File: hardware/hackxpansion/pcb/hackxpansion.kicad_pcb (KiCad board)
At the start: 4 copper layers, 52 x 69 mm, 101 parts, among them CN1 533981471, CN2 533981471, CN3 533981471, CN4 533981471, IC1 ADS7128IRTET, J1 Conn_01x03_MountingPin, J2 USB_C_Receptacle_USB2.0_14P, Q1 BSS138, Q2 2N7002, SW1 SW_Push, SW2 SW_Push, SW3 SW_On_Off, U2 RP2354B, U5 SPX3819M5-L-3-3, U7 BQ24075RGT, U8 USBLC6-2SC6, Y1 ABM8-272-T3

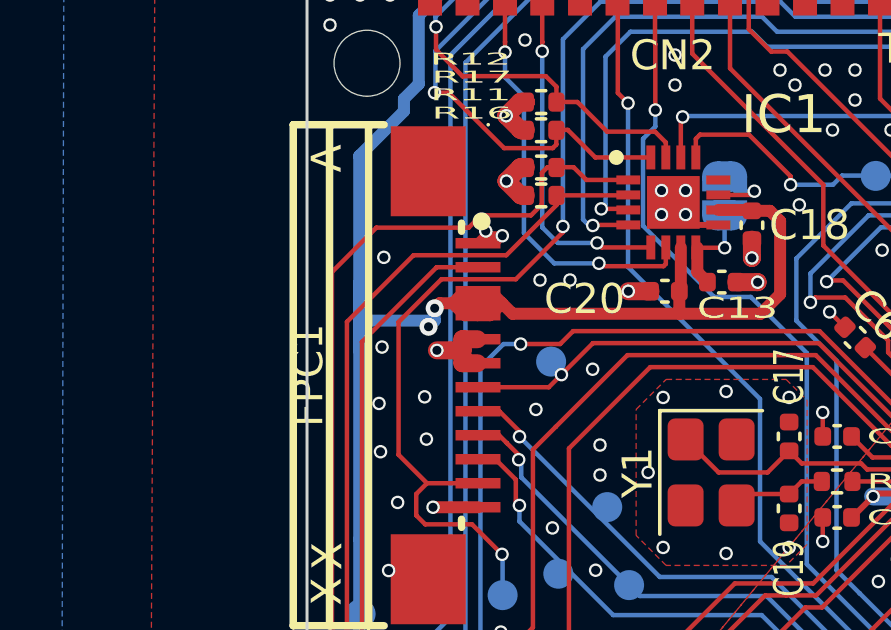
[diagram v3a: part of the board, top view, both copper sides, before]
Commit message: fixed unconnected 3v3 via next to display
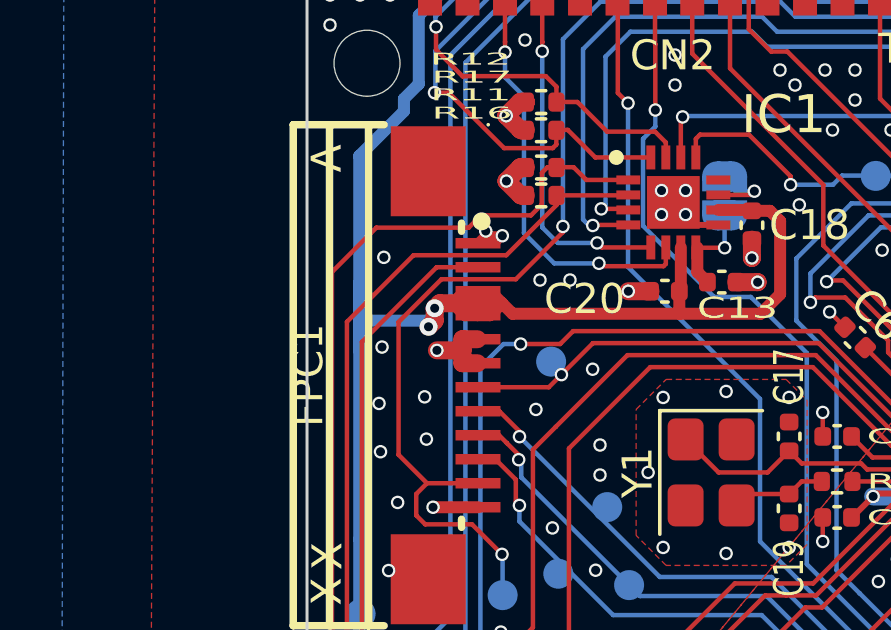
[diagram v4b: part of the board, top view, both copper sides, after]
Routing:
- net /+3V3: track 294.9 -> 295.6 mm
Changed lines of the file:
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@@
+	)
+	(segment
+		(start 106.73 72.9)
+		(end 106.29246 72.9)
+		(width 0.6)
+		(layer "F.Cu")
+		(net "/+3V3")
 	)
 	(segment
@@
 	)
 	(segment
+		(start 134.779998 63.587538)
+		(end 134.779998 62.66)
+		(width 0.4)
+		(layer "F.Cu")
+		(net "/+3V3")
+	)
+	(segment
+		(start 114.290003 73.25)
+		(end 116.99 73.25)
+		(width 0.4)
+		(layer "F.Cu")
+		(net "/+3V3")
+	)
+	(segment
+		(start 127.340001 85.24)
+		(end 127.340002 86.159999)
+		(width 0.15)
+		(layer "F.Cu")
+		(net "/+3V3")
+	)
+	(segment
+		(start 123.195 96.015001)
+		(end 123.195 96.782538)
+		(width 0.4)
+		(layer "F.Cu")
+		(net "/+3V3")
+	)
+	(segment
+		(start 132.736502 76.439999)
+		(end 133.440002 76.440001)
+		(width 0.15)
+		(layer "F.Cu")
+		(net "/+3V3")
+	)
+	(segment
+		(start 108.37 72.9)
+		(end 108.02 72.55)
+		(width 0.4)
+		(layer "F.Cu")
+		(net "/+3V3")
+	)
+	(segment
+		(start 134.588768 63.778768)
+		(end 134.779998 63.587538)
+		(width 0.4)
+		(layer "F.Cu")
+		(net "/+3V3")
+	)
+	(segment
+		(start 130.040002 73.743499)
+		(end 130.040003 74.54)
+		(width 0.2)
+		(layer "F.Cu")
+		(net "/+3V3")
+	)
+	(segment
+		(start 106.93 84.13)
+		(end 104.62 84.13)
+		(width 0.15)
+		(layer "F.Cu")
+		(net "/+3V3")
+	)
+	(segment
+		(start 151.21 97.136168)
+		(end 151.216029 97.142197)
+		(width 0.4)
+		(layer "F.Cu")
+		(net "/+3V3")
+	)
+	(segment
+		(start 107.13 73.3)
+		(end 106.73 72.9)
+		(width 0.4)
+		(layer "F.Cu")
+		(net "/+3V3")
+	)
+	(segment
+		(start 127.640002 83.536501)
+		(end 127.640001 84.94)
+		(width 0.15)
+		(layer "F.Cu")
+		(net "/+3V3")
+	)
+	(segment
+		(start 131.940002 79.639999)
+		(end 132.740003 79.64)
+		(width 0.2)
+		(layer "F.Cu")
+		(net "/+3V3")
+	)
+	(segment
+		(start 126.040002 73.743499)
+		(end 126.040003 72.64)
+		(width 0.15)
+		(layer "F.Cu")
+		(net "/+3V3")
+	)
+	(segment
+		(start 116.7 69.82)
+		(end 116.67 69.79)
+		(width 0.4)
+		(layer "F.Cu")
+		(net "/+3V3")
+	)
+	(segment
+		(start 124.040002 83.940001)
+		(end 123.340002 84.64)
+		(width 0.15)
+		(layer "F.Cu")
+		(net "/+3V3")
+	)
+	(segment
+		(start 105.920009 73.684293)
+		(end 106.125 73.479302)
+		(width 0.6)
+		(layer "F.Cu")
+		(net "/+3V3")
+	)
+	(segment
+		(start 133.190003 79.64)
+		(end 133.590002 79.240001)
+		(width 0.15)
+		(layer "F.Cu")
+		(net "/+3V3")
+	)
+	(segment
+		(start 132.140001 85.659999)
+		(end 132.140001 85.030001)
+		(width 0.15)
+		(layer "F.Cu")
+		(net "/+3V3")
+	)
+	(segment
+		(start 108.32 83.87)
+		(end 107.19 83.87)
+		(width 0.15)
+		(layer "F.Cu")
+		(net "/+3V3")
+	)
+	(segment
+		(start 114.33 72.45)
+		(end 114.33 71.04)
+		(width 0.4)
+		(layer "F.Cu")
+		(net "/+3V3")
+	)
+	(segment
+		(start 133.890002 81.16)
+		(end 133.810003 81.239999)
+		(width 0.2)
+		(layer "F.Cu")
+		(net "/+3V3")
+	)
+	(segment
+		(start 108.33 83.86)
+		(end 108.32 83.87)
+		(width 0.15)
+		(layer "F.Cu")
+		(net "/+3V3")
+	)
+	(segment
+		(start 117.3 69.82)
+		(end 116.7 69.82)
+		(width 0.4)
+		(layer "F.Cu")
+		(net "/+3V3")
+	)
+	(segment
 		(start 106.29246 72.9)
 		(end 106.125 73.06746)
-		(width 0.4)
-		(layer "F.Cu")
-		(net "/+3V3")
-	)
-	(segment
-		(start 134.779998 63.587538)
-		(end 134.779998 62.66)
-		(width 0.4)
-		(layer "F.Cu")
-		(net "/+3V3")
-	)
-	(segment
-		(start 114.290003 73.25)
-		(end 116.99 73.25)
-		(width 0.4)
-		(layer "F.Cu")
-		(net "/+3V3")
-	)
-	(segment
-		(start 127.340001 85.24)
-		(end 127.340002 86.159999)
-		(width 0.15)
-		(layer "F.Cu")
-		(net "/+3V3")
-	)
-	(segment
-		(start 123.195 96.015001)
-		(end 123.195 96.782538)
-		(width 0.4)
-		(layer "F.Cu")
-		(net "/+3V3")
-	)
-	(segment
-		(start 132.736502 76.439999)
-		(end 133.440002 76.440001)
-		(width 0.15)
-		(layer "F.Cu")
-		(net "/+3V3")
-	)
-	(segment
-		(start 108.37 72.9)
-		(end 108.02 72.55)
-		(width 0.4)
-		(layer "F.Cu")
-		(net "/+3V3")
-	)
-	(segment
-		(start 134.588768 63.778768)
-		(end 134.779998 63.587538)
-		(width 0.4)
-		(layer "F.Cu")
-		(net "/+3V3")
-	)
-	(segment
-		(start 130.040002 73.743499)
-		(end 130.040003 74.54)
-		(width 0.2)
-		(layer "F.Cu")
-		(net "/+3V3")
-	)
-	(segment
-		(start 106.93 84.13)
-		(end 104.62 84.13)
-		(width 0.15)
-		(layer "F.Cu")
-		(net "/+3V3")
-	)
-	(segment
-		(start 151.21 97.136168)
-		(end 151.216029 97.142197)
-		(width 0.4)
-		(layer "F.Cu")
-		(net "/+3V3")
-	)
-	(segment
-		(start 107.13 73.3)
-		(end 106.73 72.9)
-		(width 0.4)
-		(layer "F.Cu")
-		(net "/+3V3")
-	)
-	(segment
-		(start 127.640002 83.536501)
-		(end 127.640001 84.94)
-		(width 0.15)
-		(layer "F.Cu")
-		(net "/+3V3")
-	)
-	(segment
-		(start 131.940002 79.639999)
-		(end 132.740003 79.64)
-		(width 0.2)
-		(layer "F.Cu")
-		(net "/+3V3")
-	)
-	(segment
-		(start 126.040002 73.743499)
-		(end 126.040003 72.64)
-		(width 0.15)
-		(layer "F.Cu")
-		(net "/+3V3")
-	)
-	(segment
-		(start 116.7 69.82)
-		(end 116.67 69.79)
-		(width 0.4)
-		(layer "F.Cu")
-		(net "/+3V3")
-	)
-	(segment
-		(start 124.040002 83.940001)
-		(end 123.340002 84.64)
-		(width 0.15)
-		(layer "F.Cu")
-		(net "/+3V3")
-	)
-	(segment
-		(start 133.190003 79.64)
-		(end 133.590002 79.240001)
-		(width 0.15)
-		(layer "F.Cu")
-		(net "/+3V3")
-	)
-	(segment
-		(start 132.140001 85.659999)
-		(end 132.140001 85.030001)
-		(width 0.15)
-		(layer "F.Cu")
-		(net "/+3V3")
-	)
-	(segment
-		(start 108.32 83.87)
-		(end 107.19 83.87)
-		(width 0.15)
-		(layer "F.Cu")
-		(net "/+3V3")
-	)
-	(segment
-		(start 114.33 72.45)
-		(end 114.33 71.04)
-		(width 0.4)
-		(layer "F.Cu")
-		(net "/+3V3")
-	)
-	(segment
-		(start 133.890002 81.16)
-		(end 133.810003 81.239999)
-		(width 0.2)
-		(layer "F.Cu")
-		(net "/+3V3")
-	)
-	(segment
-		(start 108.33 83.86)
-		(end 108.32 83.87)
-		(width 0.15)
-		(layer "F.Cu")
-		(net "/+3V3")
-	)
-	(segment
-		(start 117.3 69.82)
-		(end 116.7 69.82)
-		(width 0.4)
+		(width 0.6)
 		(layer "F.Cu")
 		(net "/+3V3")
@@
 	)
 	(segment
+		(start 106.125 73.479302)
+		(end 106.125 73.06746)
+		(width 0.6)
+		(layer "F.Cu")
+		(net "/+3V3")
+	)
+	(segment
 		(start 148.079998 94.77)
 		(end 148.529998 95.22)
@@
 		(layer "F.Cu")
 		(net "/+3V3")
-	)
-	(segment
-		(start 106.73 72.9)
-		(end 106.29246 72.9)
-		(width 0.4)
-		(layer "F.Cu")
-		(net "/+3V3")

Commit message: updated led resistor
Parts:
- R25: value 10k -> 1k5

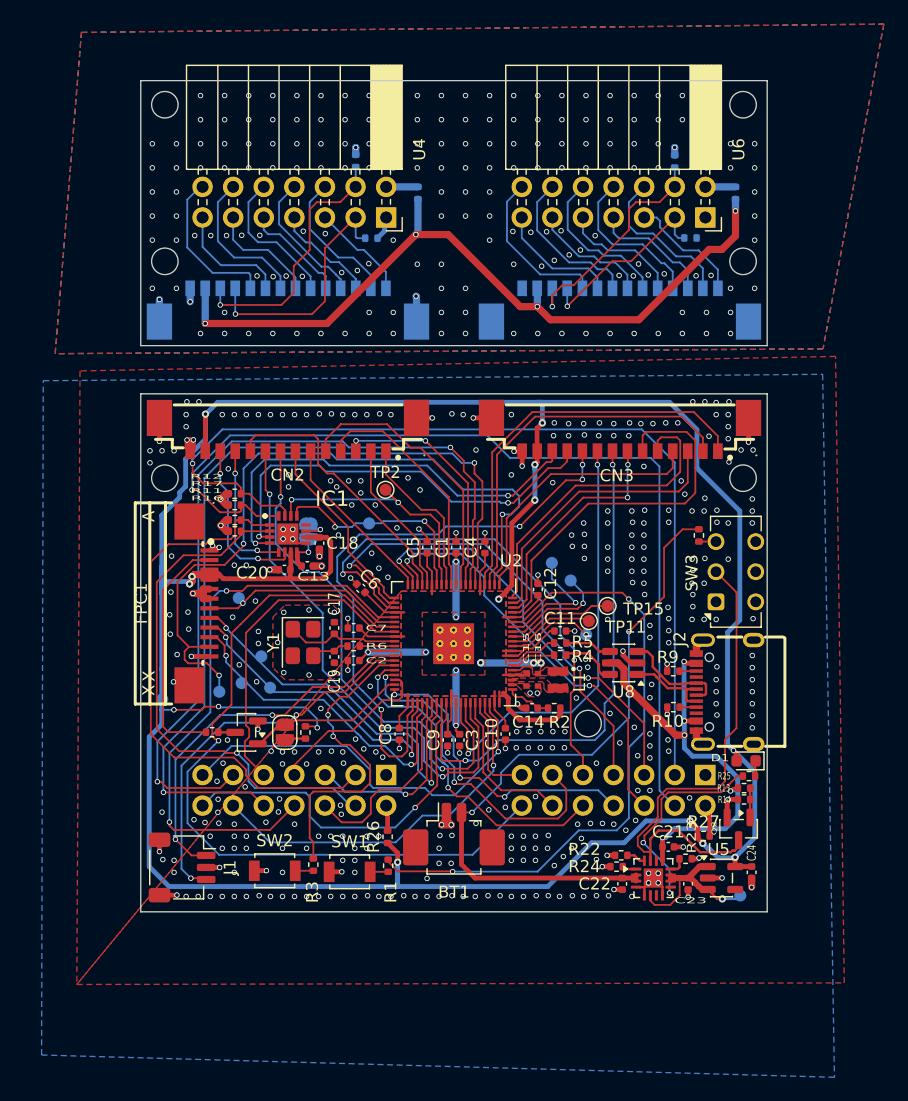
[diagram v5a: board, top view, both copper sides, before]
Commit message: changed bom, added v cut
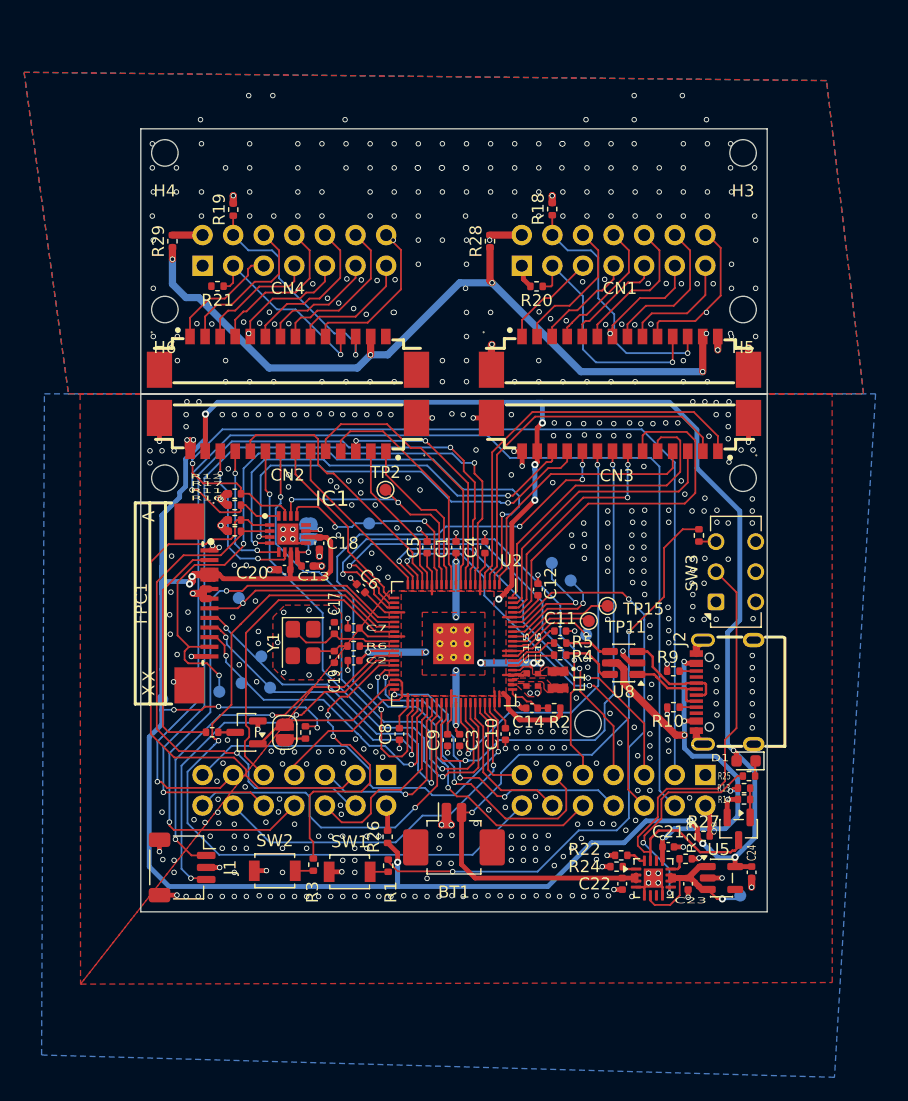
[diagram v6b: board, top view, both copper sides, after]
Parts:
- CN1, CN4, H3, H4, H5, H6, R18, R19, R20, R21, R28, R29: moved to F.Cu
- U4, U6: moved to B.Cu
- moved H3 48.2 mm to (151.9, 37.9), turned to 180 degrees
- moved H4 48.2 mm to (103.9, 37.9), turned to 180 degrees
- moved H5 48.2 mm to (151.9, 50.9), turned to 180 degrees
- moved H6 48.2 mm to (103.9, 50.9), turned to 180 degrees
- moved R29 46.9 mm to (104.5, 45.2)
- moved U6 41.9 mm to (107.0, 47.3)
- moved R21 39.5 mm to (108.2, 49.0), turned to 180 degrees
- moved R19 36.9 mm to (109.5, 42.6)
- moved CN1 27.8 mm to (141.6, 54.5), turned to 0 degrees
- moved CN4 27.8 mm to (114.1, 54.5), turned to 0 degrees
- moved R18 16.8 mm to (136.0, 42.6)
- moved R20 14.3 mm to (134.7, 49.0), turned to 180 degrees
- moved U4 11.9 mm to (133.5, 47.3)
- moved R28 7.19 mm to (130.9, 45.2)
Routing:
- net /Connector Daughter Mod2/bank.GPIO9: vias 0 -> 1
- net Net-(U4-3V3): vias 0 -> 1
- net /Connector Daughter Mod3/bank.GPIO9: vias 0 -> 1
- net /DAUGHT_GND: vias 184 -> 177
- net /Connector Daughter Mod3/bank.GPIO4: vias 0 -> 1
- net /Connector Daughter Mod2/bank.GPIO6: vias 0 -> 1
- net /DAUGHT_+3V3: vias 4 -> 6
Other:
- board size 52 x 69 mm -> 52 x 65 mm
